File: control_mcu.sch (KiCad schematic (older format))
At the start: 10 parts, among them U1 ATtiny841-SSU

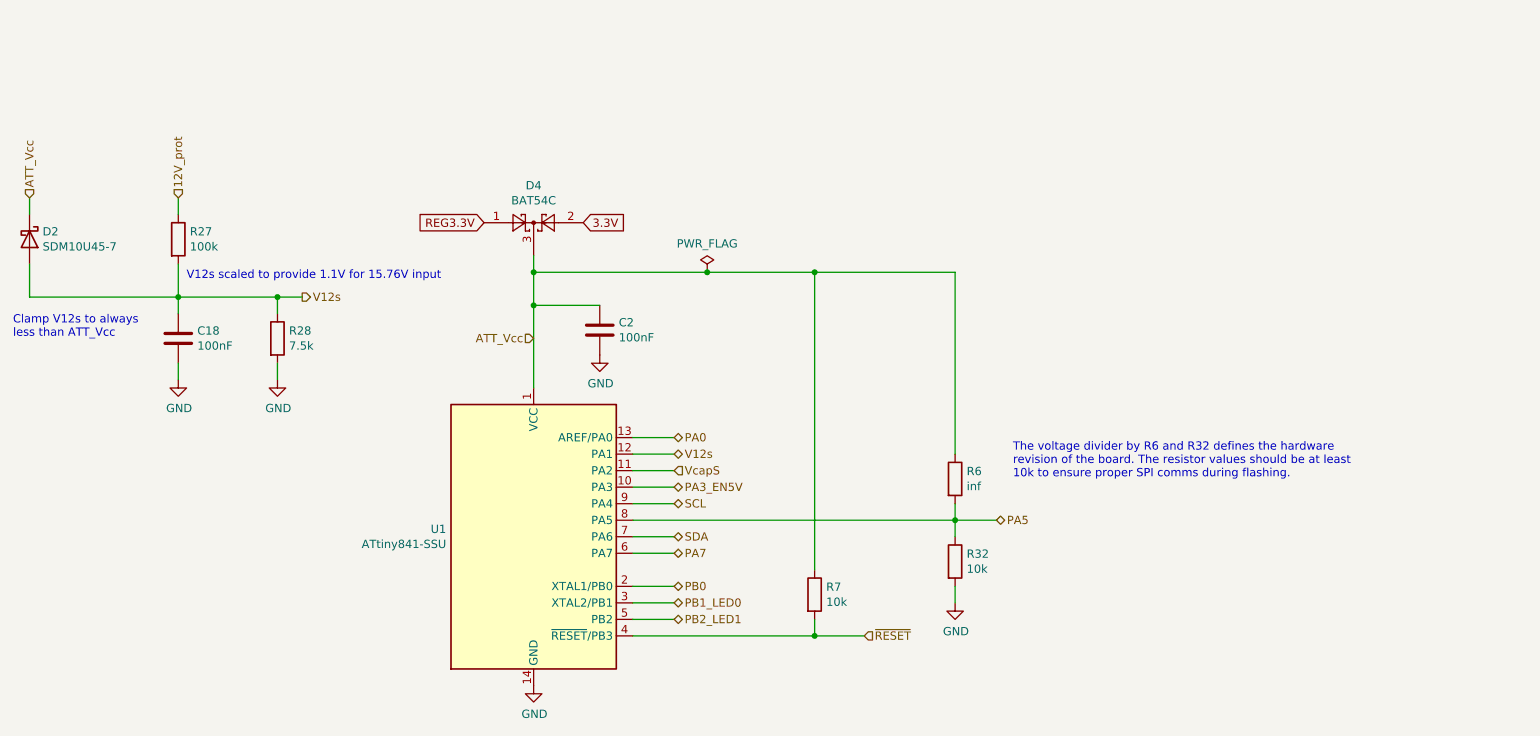
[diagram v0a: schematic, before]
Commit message: Isolated CAN bus implementation
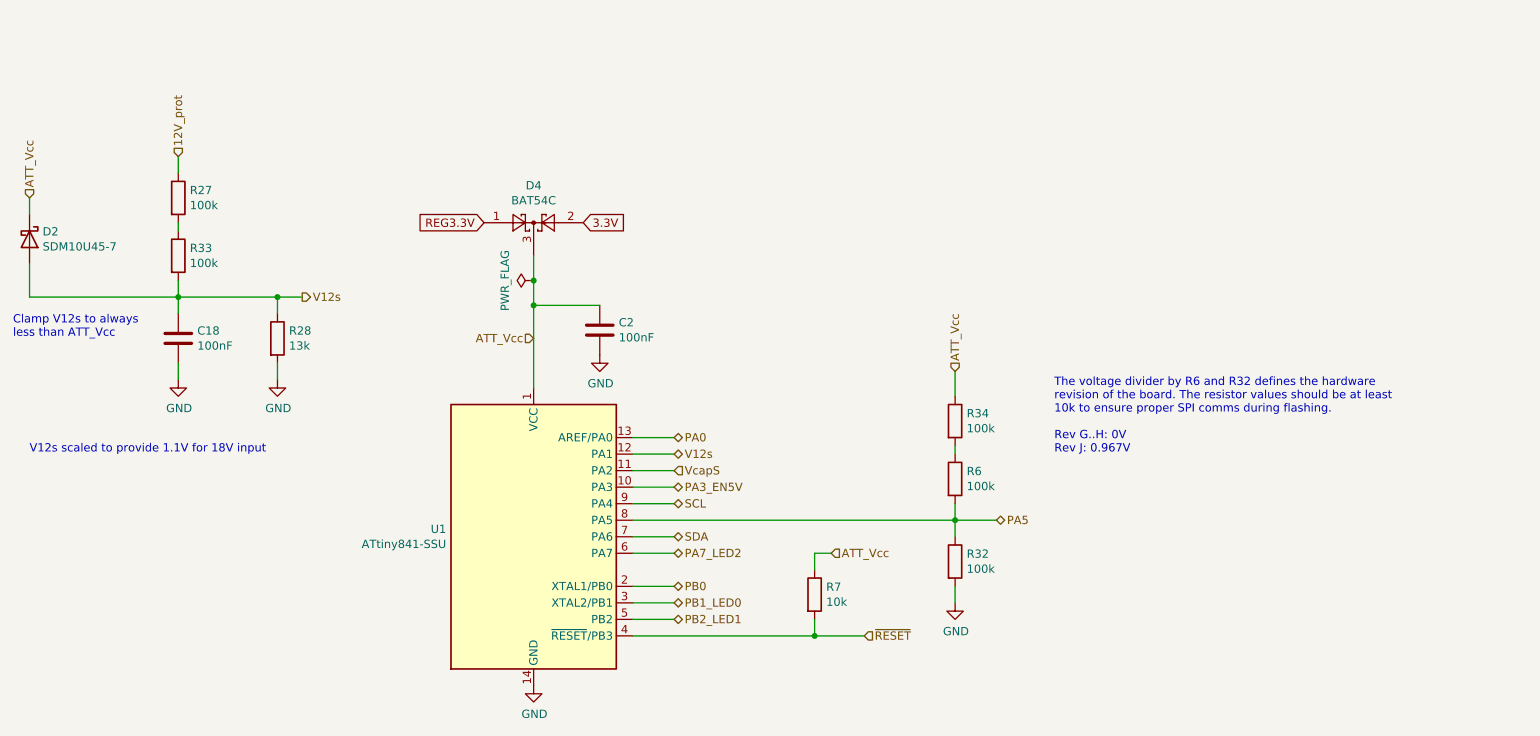
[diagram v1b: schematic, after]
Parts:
- added R33, R34: 100k, Resistor_SMD:R_0603_1608Metric, symbol Device:R
- C18, C2: footprint Capacitor_SMD:C_0603_1608Metric_Pad1.05x0.95mm_HandSolder -> Capacitor_SMD:C_0603_1608Metric
- R27: footprint Resistor_SMD:R_0603_1608Metric_Pad1.05x0.95mm_HandSolder -> Resistor_SMD:R_0603_1608Metric; LCSC C25803 -> (none)
- R28: value 7.5k -> 13k; footprint Resistor_SMD:R_0603_1608Metric_Pad1.05x0.95mm_HandSolder -> Resistor_SMD:R_0603_1608Metric; LCSC C23234 -> (none)
- R32: value 10k -> 100k; footprint Resistor_SMD:R_0603_1608Metric_Pad1.05x0.95mm_HandSolder -> Resistor_SMD:R_0603_1608Metric; LCSC C25804 -> (none)
- R6: value inf -> 100k; footprint Resistor_SMD:R_0603_1608Metric_Pad1.05x0.95mm_HandSolder -> Resistor_SMD:R_0603_1608Metric
- R7: footprint Resistor_SMD:R_0603_1608Metric_Pad1.05x0.95mm_HandSolder -> Resistor_SMD:R_0603_1608Metric
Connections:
- net ATT_Vcc: now also R34.1; no longer R6.1
- net V12s: now also R33.2; no longer R27.2
- net PA7 renamed PA7_LED2
- new net: R27.2, R33.1
- new net: R34.2, R6.1
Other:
- note added: "The voltage divider by R6 and R32 defines the hardware\nrevision of the board. The resistor values should be at least\n10k to ensure proper SPI comms during flashing.\n\nRev G..H: 0V\nRev J: 0.967V"
- note added: "V12s scaled to provide 1.1V for 18V input"
- note removed: "The voltage divider by R6 and R32 defines the hardware\nrevision of the board. The resistor values should be at least\n10k to ensure proper SPI comms during flashing."
- note removed: "V12s scaled to provide 1.1V for 15.76V input"
- moved on the sheet: R27

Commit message: Parts updated to match JLCPCB availability
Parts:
- D2: value SDM10U45-7 -> PSBD521S-40; LCSC C150997 -> C168633
- D4: LCSC C14308 -> C375703
- R27, R32, R33, R34, R6: LCSC (none) -> C25803
- R28: LCSC (none) -> C22797
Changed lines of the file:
@@
 F 2 "Package_TO_SOT_SMD:SOT-23" H 3875 2725 50  0001 L CNN
 F 3 "http://www.diodes.com/_files/datasheets/ds11005.pdf" H 3720 2600 50  0001 C CNN
-F 4 "C14308" H 3800 2600 50  0001 C CNN "LCSC"
+F 4 "C375703" H 3800 2600 50  0001 C CNN "LCSC"
 	1    3800 2600
 	1    0    0    -1
@@
 F 2 "Resistor_SMD:R_0603_1608Metric" V 6280 4650 50  0001 C CNN
 F 3 "~" H 6350 4650 50  0001 C CNN
-F 4 "" H 6350 4650 50  0001 C CNN "LCSC"
+F 4 "C25803" H 6350 4650 50  0001 C CNN "LCSC"
 	1    6350 4650
 	1    0    0    -1
@@
 F 2 "Resistor_SMD:R_0603_1608Metric" V 6280 4150 50  0001 C CNN
 F 3 "~" H 6350 4150 50  0001 C CNN
+F 4 "C25803" H 6350 4150 50  0001 C CNN "LCSC"
 	1    6350 4150
 	1    0    0    -1
@@
 P 750 2700
 F 0 "D2" V 704 2779 50  0000 L CNN
-F 1 "SDM10U45-7" V 795 2779 50  0000 L CNN
+F 1 "PSBD521S-40" V 795 2779 50  0000 L CNN
 F 2 "Diode_SMD:D_SOD-523" H 750 2700 50  0001 C CNN
 F 3 "~" H 750 2700 50  0001 C CNN
-F 4 "C150997" H 750 2700 50  0001 C CNN "LCSC"
+F 4 "C168633" H 750 2700 50  0001 C CNN "LCSC"
 	1    750  2700
 	0    1    1    0
@@
 F 2 "Resistor_SMD:R_0603_1608Metric" V 2180 3300 50  0001 C CNN
 F 3 "~" H 2250 3300 50  0001 C CNN
-F 4 "" H 2250 3300 50  0001 C CNN "LCSC"
+F 4 "C22797" H 2250 3300 50  0001 C CNN "LCSC"
 	1    2250 3300
 	1    0    0    -1
@@
 F 2 "Resistor_SMD:R_0603_1608Metric" V 1580 2450 50  0001 C CNN
 F 3 "~" H 1650 2450 50  0001 C CNN
-F 4 "" H 1650 2450 50  0001 C CNN "LCSC"
+F 4 "C25803" H 1650 2450 50  0001 C CNN "LCSC"
 	1    1650 2450
 	1    0    0    -1
@@
 F 2 "Resistor_SMD:R_0603_1608Metric" V 1580 2800 50  0001 C CNN
 F 3 "~" H 1650 2800 50  0001 C CNN
-F 4 "" H 1650 2800 50  0001 C CNN "LCSC"
+F 4 "C25803" H 1650 2800 50  0001 C CNN "LCSC"
 	1    1650 2800
 	1    0    0    -1
@@
 F 2 "Resistor_SMD:R_0603_1608Metric" V 6280 3800 50  0001 C CNN
 F 3 "~" H 6350 3800 50  0001 C CNN
+F 4 "C25803" H 6350 3800 50  0001 C CNN "LCSC"
 	1    6350 3800
 	1    0    0    -1

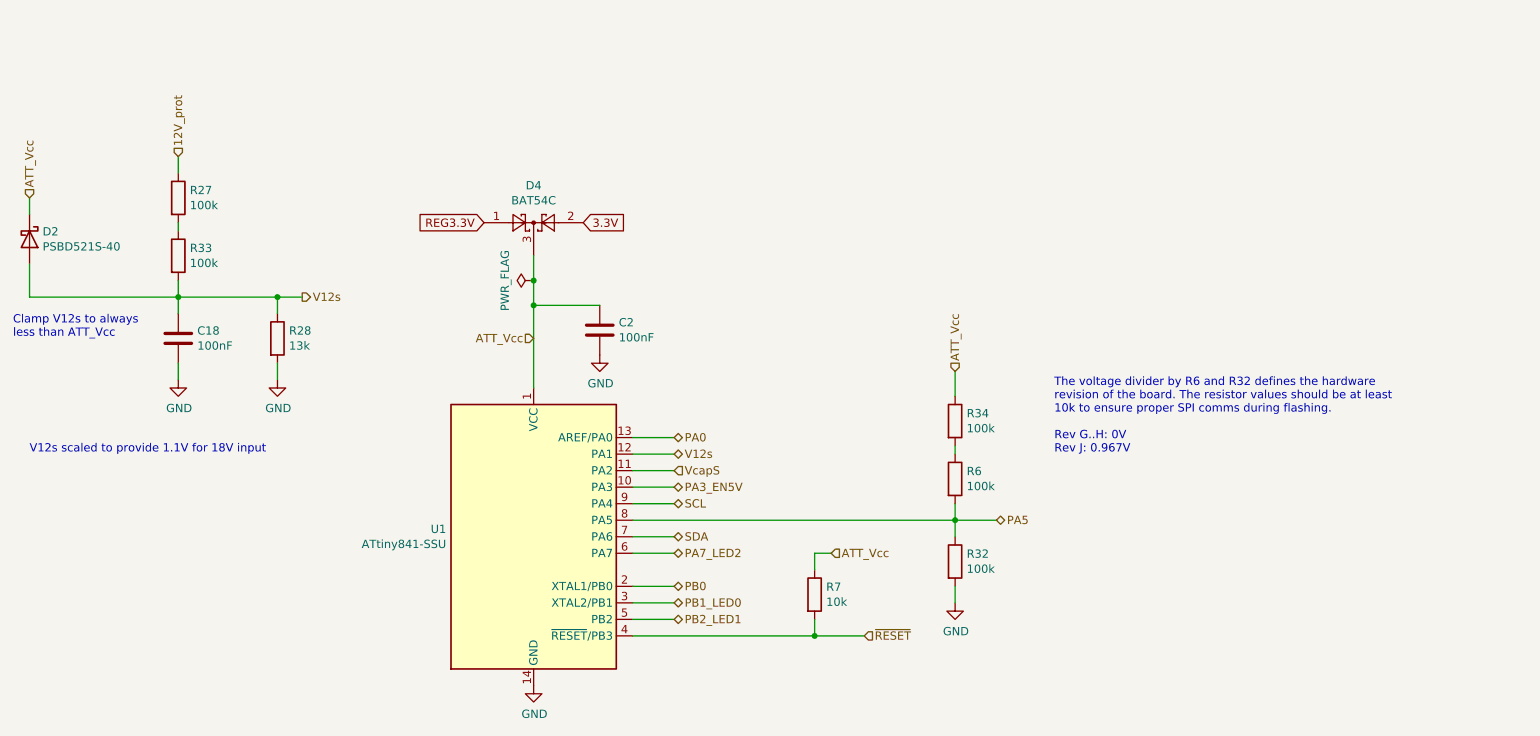
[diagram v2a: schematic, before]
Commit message: Update components according to JLCPCB availability
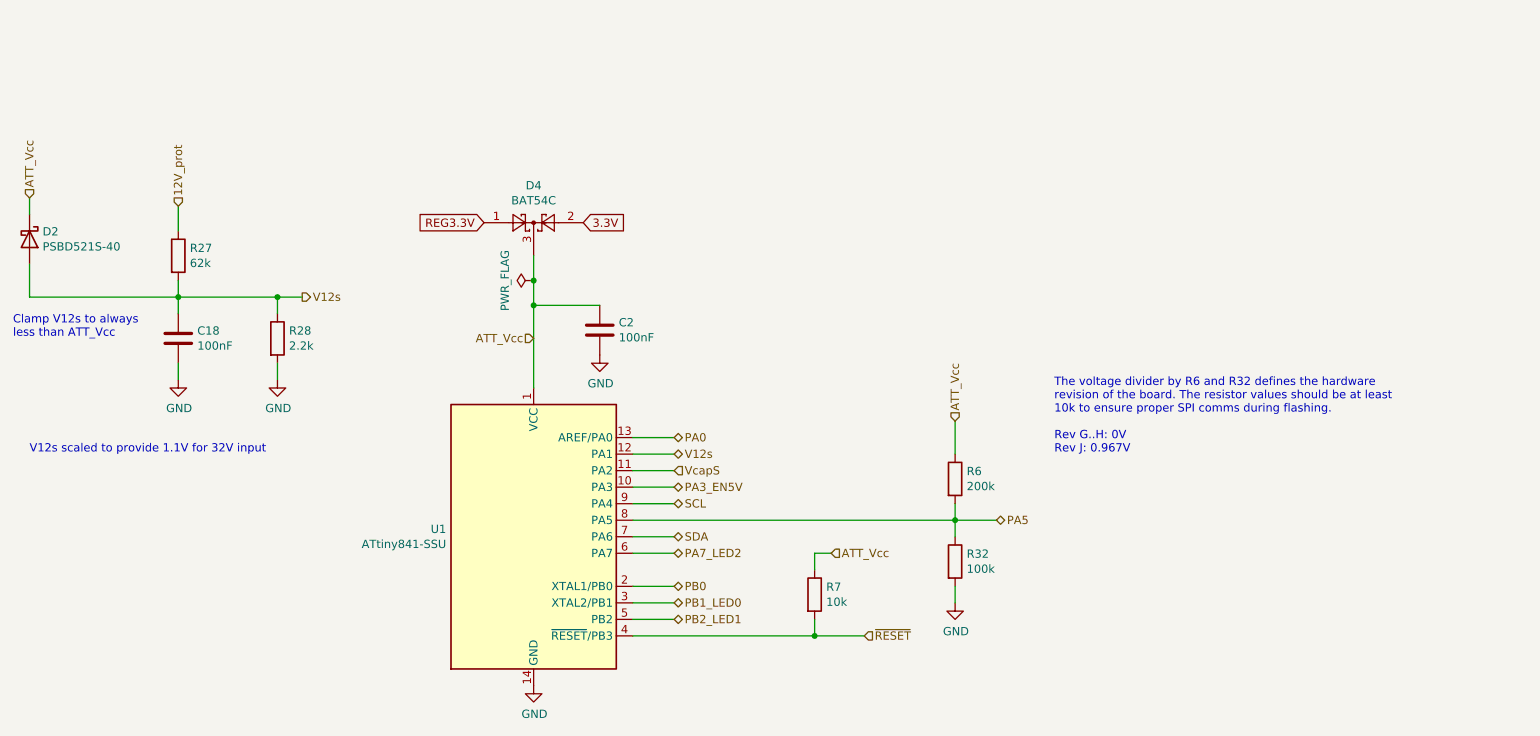
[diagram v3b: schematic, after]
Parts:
- removed R33, R34: 100k, Resistor_SMD:R_0603_1608Metric, symbol Device:R
- R27: value 100k -> 62k; LCSC C25803 -> C23221
- R28: value 13k -> 2.2k; LCSC C22797 -> C4190
- R6: value 100k -> 200k; LCSC C25803 -> C25811
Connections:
- net ATT_Vcc: now also R6.1
- net V12s: now also R27.2
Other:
- note added: "V12s scaled to provide 1.1V for 32V input"
- note removed: "V12s scaled to provide 1.1V for 18V input"
- moved on the sheet: R27
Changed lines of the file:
@@
 P 6350 4150
 F 0 "R6" H 6420 4196 50  0000 L CNN
-F 1 "100k" H 6420 4105 50  0000 L CNN
+F 1 "200k" H 6420 4105 50  0000 L CNN
 F 2 "Resistor_SMD:R_0603_1608Metric" V 6280 4150 50  0001 C CNN
 F 3 "~" H 6350 4150 50  0001 C CNN
-F 4 "C25803" H 6350 4150 50  0001 C CNN "LCSC"
+F 4 "C25811" H 6350 4150 50  0001 C CNN "LCSC"
 	1    6350 4150
 	1    0    0    -1
@@
 ATT_Vcc
 Text Notes 750  4000 0    50   ~ 0
-V12s scaled to provide 1.1V for 18V input
+V12s scaled to provide 1.1V for 32V input
 Wire Wire Line
 	2250 3050 2400 3050
@@
 AR Path="/5C33FF90/5CFB31B2" Ref="R28"  Part="1"
 F 0 "R28" H 2320 3346 50  0000 L CNN
-F 1 "13k" H 2320 3255 50  0000 L CNN
+F 1 "2.2k" H 2320 3255 50  0000 L CNN
 F 2 "Resistor_SMD:R_0603_1608Metric" V 2180 3300 50  0001 C CNN
 F 3 "~" H 2250 3300 50  0001 C CNN
-F 4 "C22797" H 2250 3300 50  0001 C CNN "LCSC"
+F 4 "C4190" H 2250 3300 50  0001 C CNN "LCSC"
 	1    2250 3300
 	1    0    0    -1
@@
 	1    0    0    -1
 $EndComp
-Wire Wire Line
-	1650 2200 1650 2300
-Text HLabel 1650 2200 1    50   Input ~ 0
+Text HLabel 1650 2500 1    50   Input ~ 0
 12V_prot
 Wire Wire Line
@@
 L Device:R R?
 U 1 1 5CF4FF7C
-P 1650 2450
+P 1650 2800
 AR Path="/5CF4FF7C" Ref="R?"  Part="1"
 AR Path="/5C33FF90/5CF4FF7C" Ref="R27"  Part="1"
-F 0 "R27" H 1720 2496 50  0000 L CNN
-F 1 "100k" H 1720 2405 50  0000 L CNN
-F 2 "Resistor_SMD:R_0603_1608Metric" V 1580 2450 50  0001 C CNN
-F 3 "~" H 1650 2450 50  0001 C CNN
-F 4 "C25803" H 1650 2450 50  0001 C CNN "LCSC"
-	1    1650 2450
+F 0 "R27" H 1720 2846 50  0000 L CNN
+F 1 "62k" H 1720 2755 50  0000 L CNN
+F 2 "Resistor_SMD:R_0603_1608Metric" V 1580 2800 50  0001 C CNN
+F 3 "~" H 1650 2800 50  0001 C CNN
+F 4 "C23221" H 1650 2800 50  0001 C CNN "LCSC"
+	1    1650 2800
 	1    0    0    -1
 $EndComp
@@
 Text HLabel 5600 4600 2    50   Input ~ 0
 ATT_Vcc
-Text HLabel 6350 3500 1    50   Input ~ 0
+Text HLabel 6350 3800 1    50   Input ~ 0
 ATT_Vcc
-Wire Wire Line
-	6350 3500 6350 3650
 Wire Wire Line
 	5500 4600 5500 4700
@@
 Wire Wire Line
 	3800 2800 3800 2950
-$Comp
-L Device:R R?
-U 1 1 5F49545C
-P 1650 2800
-AR Path="/5F49545C" Ref="R?"  Part="1"
-AR Path="/5C33FF90/5F49545C" Ref="R33"  Part="1"
-F 0 "R33" H 1720 2846 50  0000 L CNN
-F 1 "100k" H 1720 2755 50  0000 L CNN
-F 2 "Resistor_SMD:R_0603_1608Metric" V 1580 2800 50  0001 C CNN
-F 3 "~" H 1650 2800 50  0001 C CNN
-F 4 "C25803" H 1650 2800 50  0001 C CNN "LCSC"
-	1    1650 2800
-	1    0    0    -1
-$EndComp
 Wire Wire Line
-	1650 2650 1650 2600
-$Comp
-L Device:R R34
-U 1 1 5F49A3E0
-P 6350 3800
-F 0 "R34" H 6420 3846 50  0000 L CNN
-F 1 "100k" H 6420 3755 50  0000 L CNN
-F 2 "Resistor_SMD:R_0603_1608Metric" V 6280 3800 50  0001 C CNN
-F 3 "~" H 6350 3800 50  0001 C CNN
-F 4 "C25803" H 6350 3800 50  0001 C CNN "LCSC"
-	1    6350 3800
-	1    0    0    -1
-$EndComp
+	1650 2500 1650 2650
 Wire Wire Line
-	6350 3950 6350 4000
+	6350 3800 6350 4000
 $EndSCHEMATC

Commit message: Schema updated
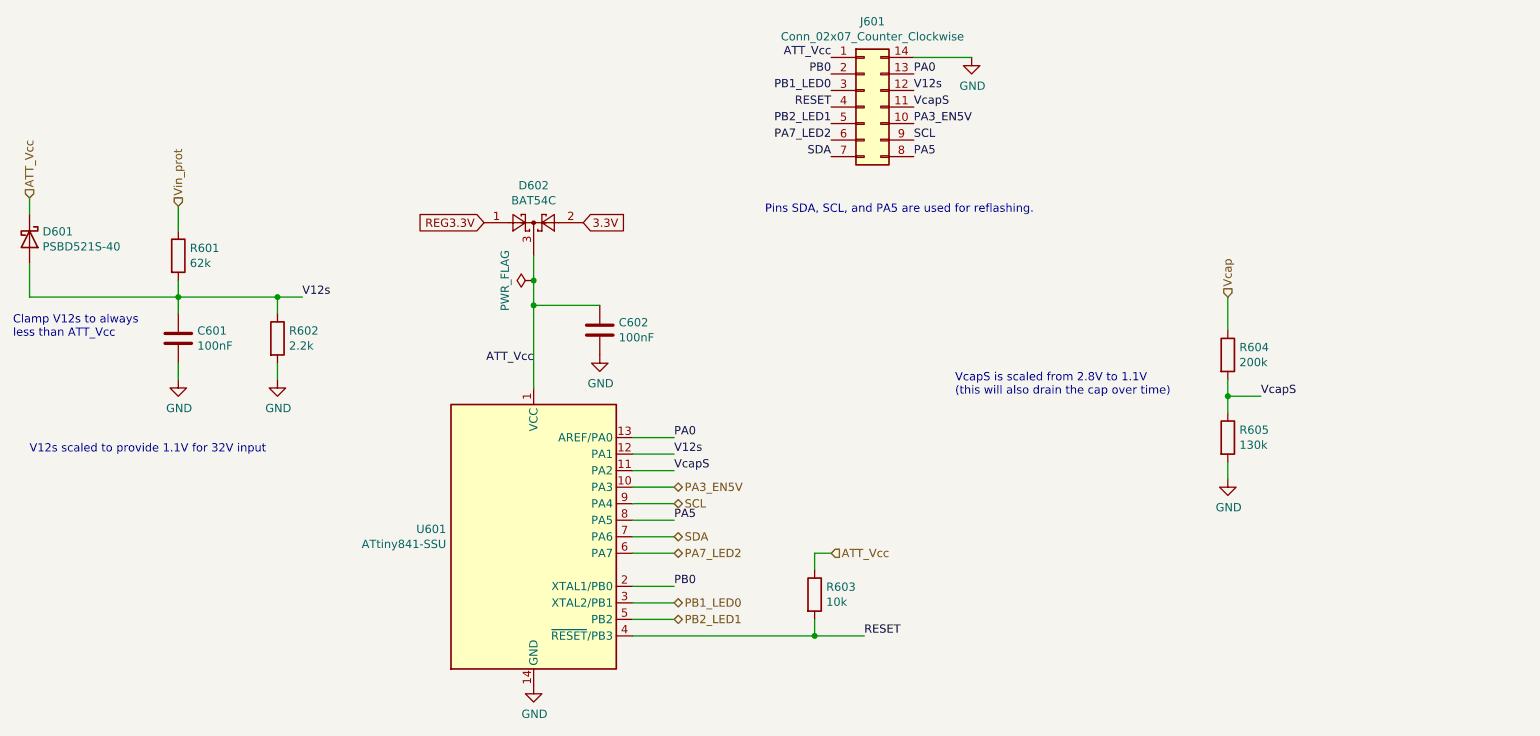
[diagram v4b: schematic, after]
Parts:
- removed R32: 100k, Resistor_SMD:R_0603_1608Metric, symbol Device:R
- removed R6: 200k, Resistor_SMD:R_0603_1608Metric, symbol Device:R
- added J601: Conn_02x07_Counter_Clockwise, custom:PinHeader_2x07_P2.54mm_Vertical_CounterClockwise, symbol Connector_Generic:Conn_02x07_Counter_Clockwise
- added R604: 200k, Resistor_SMD:R_0603_1608Metric, symbol Device:R
- added R605: 130k, Resistor_SMD:R_0603_1608Metric, symbol Device:R
- renumbered C18 to C601, C2 to C602, D2 to D601, D4 to D602, R27 to R601, R28 to R602, R7 to R603, U1 to U601
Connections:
- net ATT_Vcc: now also J601.1 (Pin_1)
- net GND: now also J601.14 (Pin_14), R605.2
- net PA0: now also J601.13 (Pin_13)
- net PA3_EN5V: now also J601.10 (Pin_10)
- net PA5: now also J601.8 (Pin_8)
- net PA7_LED2: now also J601.6 (Pin_6)
- net PB0: now also J601.2 (Pin_2)
- net PB1_LED0: now also J601.3 (Pin_3)
- net PB2_LED1: now also J601.5 (Pin_5)
- net SCL: now also J601.9 (Pin_9)
- net SDA: now also J601.7 (Pin_7)
- net V12s: now also J601.12 (Pin_12)
- net VcapS: now also J601.11 (Pin_11), R604.2, R605.1
- net 12V_prot renamed Vin_prot
- net ~RESET~ renamed RESET
- net RESET: now also J601.4 (Pin_4)
- new net Vcap: R604.1
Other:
- note added: "Pins SDA, SCL, and PA5 are used for reflashing.\n"
- note added: "VcapS is scaled from 2.8V to 1.1V\n(this will also drain the cap over time)"
- note removed: "The voltage divider by R6 and R32 defines the hardware\nrevision of the board. The resistor values should be at least\n10k to ensure proper SPI comms during flashing.\n\nRev G..H: 0V\nRev J: 0.967V"
